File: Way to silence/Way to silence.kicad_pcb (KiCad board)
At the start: 2 copper layers, 59.3 x 38.1 mm, 66 parts, among them J1 SD Card Connector, J2 Amplificator_Terminal, J3 5V_Terminal, J4 Battery_Terminal, J5 LEDS Port, Q1 BC817, Q2 BC817, SW1 SW_SPDT, SW3 SW_SPST, U1 ESP32-WROOM-32-N16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

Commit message: [RTN] Routing in progress
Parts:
- moved C2 16.9 mm to (78.4, 79.8), turned to 180 degrees
- moved C9 5.16 mm to (91.4, 66.5)
- moved C13 3.23 mm to (94.7, 66.5)
- moved C12 3.10 mm to (96.5, 66.5)
- moved R8 1.05 mm to (78.4, 81.4)
- moved U4 0.69 mm to (77.9, 61.1)
- moved FB1 0.37 mm to (74.4, 61.1)
- moved SW3 0.10 mm to (103.1, 58.7)
- turned C10 to 180 degrees
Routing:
- net /USB to Uart/USB +5V: track 0.00 -> 90.6 mm, vias 0 -> 4
- net +5V: track 0.00 -> 40.4 mm, vias 0 -> 1
- net +3.3V: track 0.00 -> 36.9 mm, vias 0 -> 4
- net /ESP_TX: track 0.00 -> 34.6 mm, vias 0 -> 2
- net /ESP_RX: track 0.00 -> 33.2 mm, vias 0 -> 2
- net Net-(U2-BAT): track 0.00 -> 31.5 mm, vias 0 -> 2
- net /Battery Management/VOUT: track 0.00 -> 29.9 mm
- net /Battery Management/BAT: track 0.00 -> 28.0 mm, vias 0 -> 2
- net /ESP_IO0: track 0.00 -> 27.9 mm
- net /ESP_EN: track 0.00 -> 24.4 mm
- net /ESP_IO13: track 0.00 -> 24.2 mm
- net Net-(U2-SW): track 0.00 -> 23.8 mm, vias 0 -> 4
- net Net-(U2-LED2): track 0.00 -> 23.5 mm
- net Net-(D1-K): track 0.00 -> 18.5 mm
- net Net-(U2-LED1): track 0.00 -> 16.3 mm, vias 0 -> 2
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
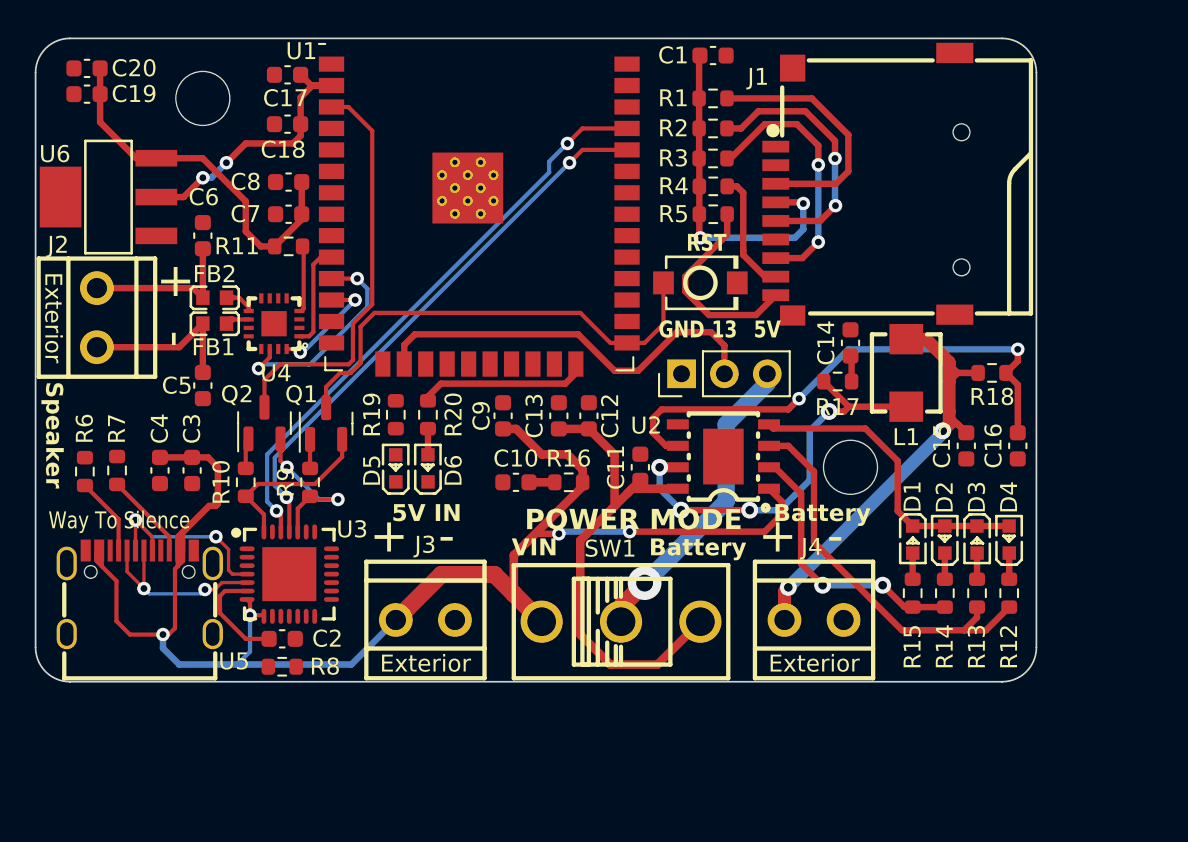
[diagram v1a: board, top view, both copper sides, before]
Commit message: [RTN] Non gnd completed
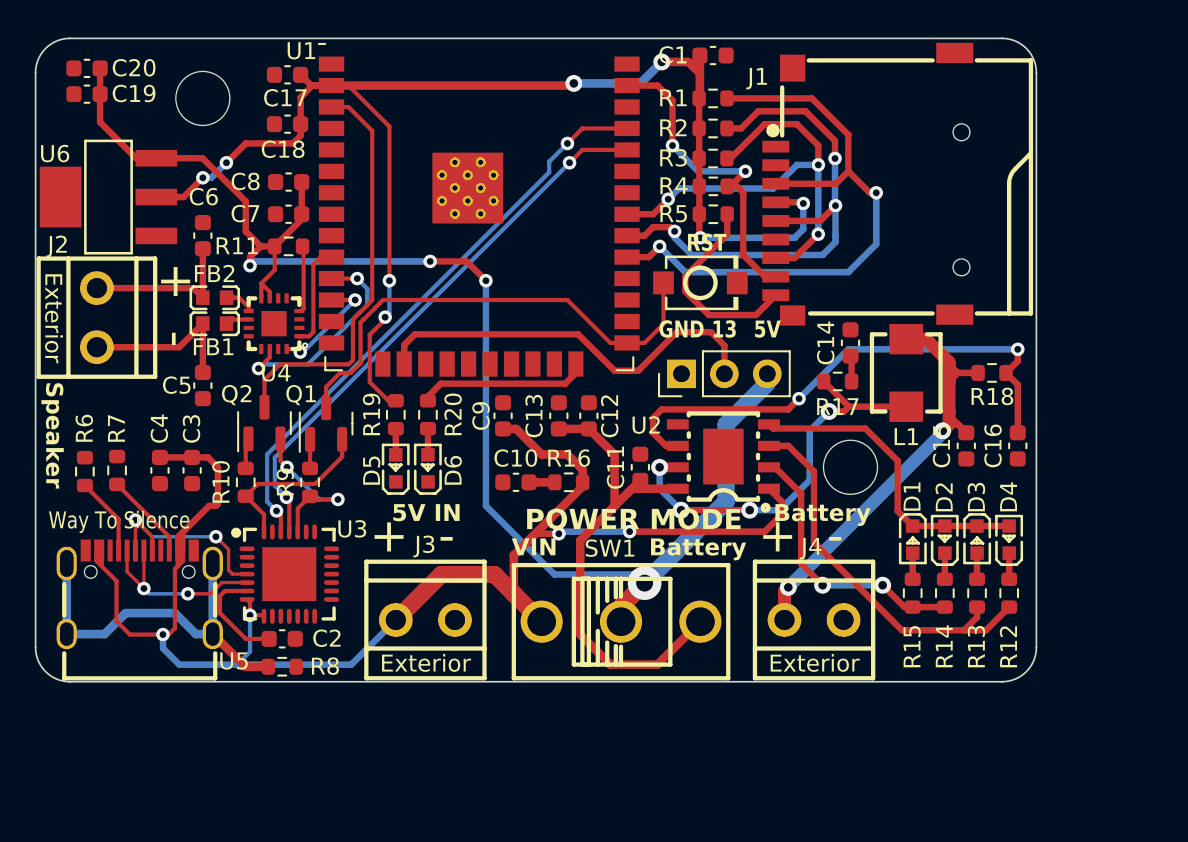
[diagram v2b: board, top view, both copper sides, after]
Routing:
- net +3.3V: track 36.9 -> 84.2 mm, vias 4 -> 8
- net +5V: track 40.4 -> 85.4 mm, vias 1 -> 4
- net /USB to Uart/SH: track 0.00 -> 22.1 mm
- net /ESP_IO5: track 14.8 -> 36.4 mm, vias 0 -> 2
- net /ESP_IO18: track 15.3 -> 31.2 mm, vias 2 -> 3
- net /ESP_IO19: track 15.4 -> 27.7 mm, vias 2 -> 3
- net /ESP_IO23: track 7.25 -> 19.4 mm, vias 0 -> 2
- net Net-(D5-A): track 0.00 -> 1.55 mm
- net /ESP_IO0: track 27.9 -> 28.7 mm

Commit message: [UDPT] Page Settings
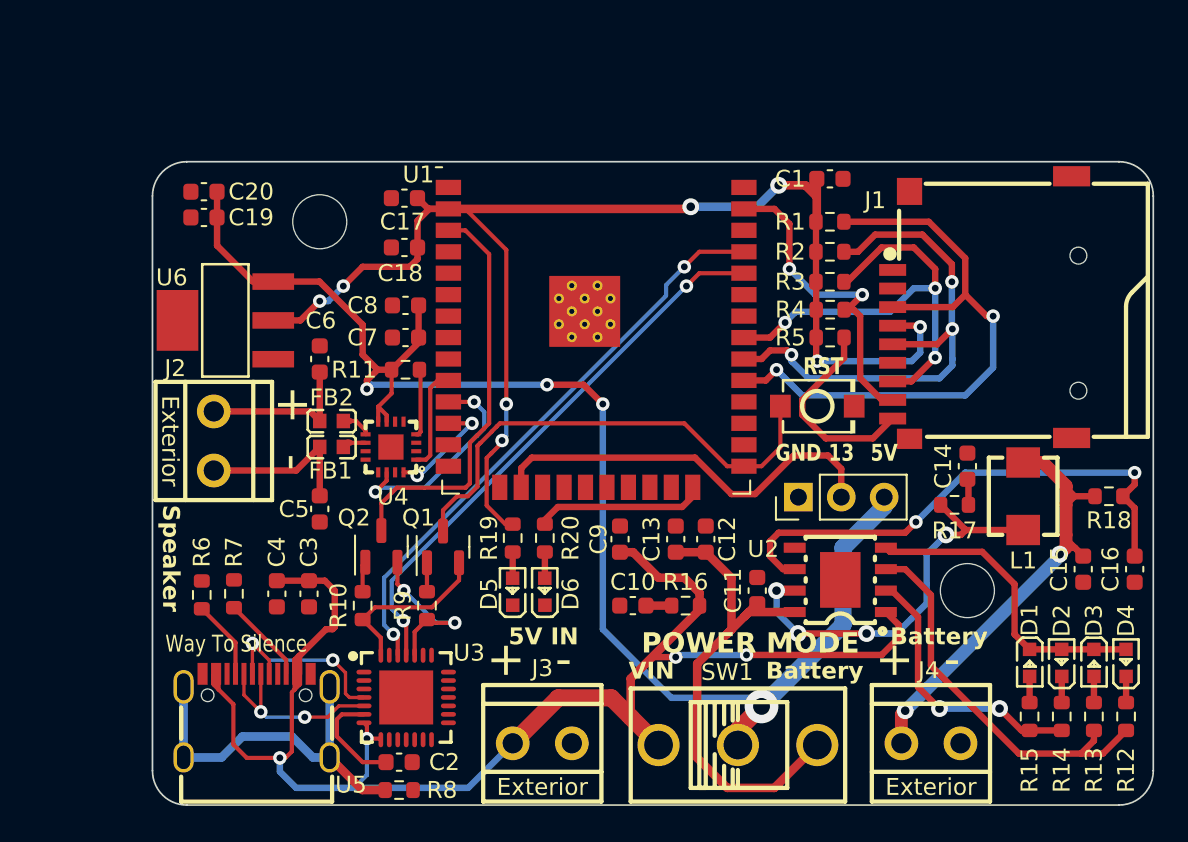
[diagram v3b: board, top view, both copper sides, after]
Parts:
- moved Q1 10.1 mm to (87.9, 74.3)
- moved R6 10.1 mm to (73.6, 77.2)
- moved R8 10.1 mm to (85.3, 88.7)
- moved SW1 10.1 mm to (105.3, 86.0)
- moved C14 10.1 mm to (118.9, 69.5)
- moved C17 10.1 mm to (85.6, 53.7)
- moved C7 10.1 mm to (85.7, 61.9)
- moved C8 10.1 mm to (85.7, 60.0)
- moved R11 10.1 mm to (85.7, 63.8)
- moved R5 10.1 mm to (110.8, 61.9)
- moved SW3 10.1 mm to (110.0, 66.0)
- moved U1 10.1 mm to (97.1, 61.0)
- moved C10 10.1 mm to (99.1, 77.8)
- moved C11 10.1 mm to (106.5, 76.9)
- moved C12 10.1 mm to (103.4, 73.9)
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
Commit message: [DRC] Seems ok
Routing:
- net GND: track 0.00 -> 74.8 mm, vias 0 -> 14
- net /ESP_IO18: track 31.2 -> 34.1 mm
- net /ESP_RX: track 33.2 -> 35.1 mm
- net /ESP_TX: track 34.6 -> 36.5 mm
- net /ESP_IO19: track 27.7 -> 29.5 mm
- net /SD Card/Card Inserted: track 12.0 -> 13.2 mm
- added copper zone on B.Cu, net GND
- added copper zone on F.Cu, net GND

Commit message: [ADD] Back Silkscreen
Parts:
- added IMAGE: LOGO, LOGO, B.Cu at (98.8, 77.3)
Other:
- board text added: "Way to silence,"
- board text added: "where whispers of the heart are heard, Beyond the clamor, where the soul's voice emerges clear, In stillness, we find clarity, in quietude, our truth appears, For in the hush of moments, the universe draws near."

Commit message: [ADD] Qr code & website
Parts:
- added G***: LOGO, LOGO, B.Cu at (76.8, 76.3)
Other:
- board text added: "juthomas.fr"

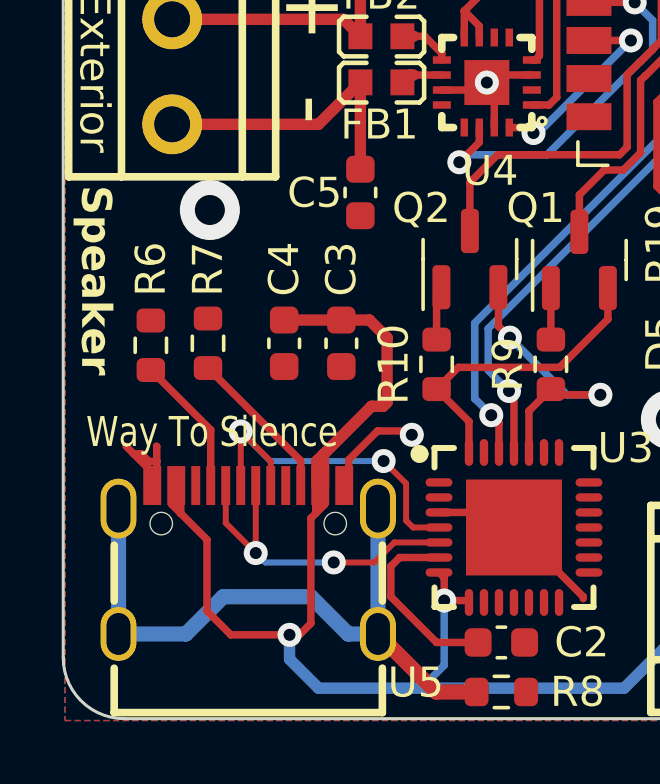
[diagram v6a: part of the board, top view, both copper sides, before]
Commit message: [FIX] LCSC Parts property
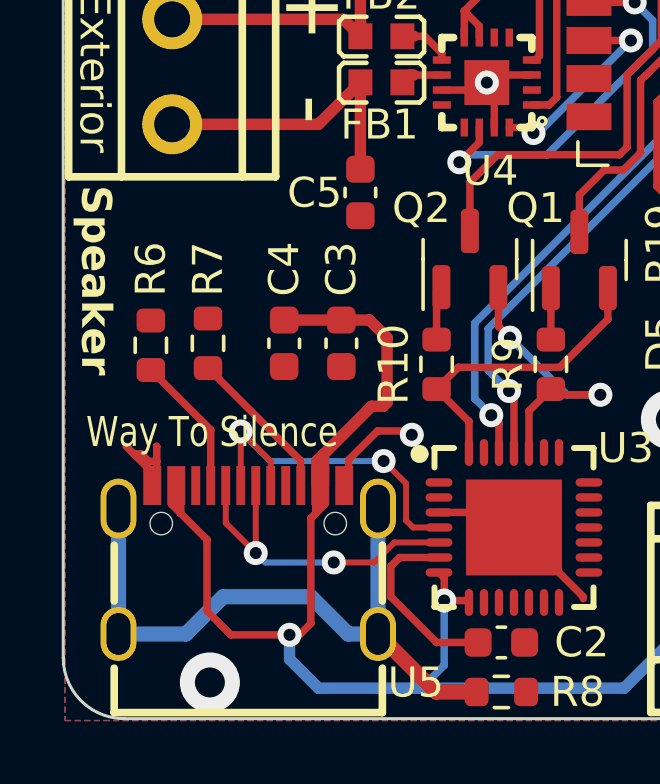
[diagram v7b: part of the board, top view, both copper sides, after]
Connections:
- net /Battery Management/BAT renamed /BMS/BAT
- net /Battery Management/VOUT renamed /BMS/VOUT
- net /USB to Uart/USB +5V renamed /USB to Uart/+5V
